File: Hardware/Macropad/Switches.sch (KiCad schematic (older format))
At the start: 49 parts, among them SW1 Rotary_Encoder_Switch, SW10 K21_1U, SW11 K11_1U, SW12 K01_1U, SW13 K42_1U, SW14 K32_1U, SW15 K22_1U, SW16 K12_1U, SW17 K02_1U, SW18 K43_1U, SW19 K33_1U, SW2 K40_1U, SW21 K23_1U, SW22 K13_1U, SW24 K03_1U, SW3 K30_1U, SW4 K20_1U, SW5 K10_1U, SW7 K00_1U, SW8 K41_1U, SW9 K31_1U

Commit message: Schematic mostly done. Started grouping components in layout
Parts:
- D10: renamed from D20; footprint Diode_SMD:D_SOD-323F -> custom_footprint_library:SOD323_HS
- D11: renamed from D23; footprint Diode_SMD:D_SOD-323F -> custom_footprint_library:SOD323_HS
- D12: renamed from D24; footprint Diode_SMD:D_SOD-323F -> custom_footprint_library:SOD323_HS
- D13: renamed from D25; footprint Diode_SMD:D_SOD-323F -> custom_footprint_library:SOD323_HS
- D14: renamed from D26; footprint Diode_SMD:D_SOD-323F -> custom_footprint_library:SOD323_HS
- D15: renamed from D27; footprint Diode_SMD:D_SOD-323F -> custom_footprint_library:SOD323_HS
- D16: renamed from D28; footprint Diode_SMD:D_SOD-323F -> custom_footprint_library:SOD323_HS
- D17: renamed from D29; footprint Diode_SMD:D_SOD-323F -> custom_footprint_library:SOD323_HS
- D18: renamed from D30; footprint Diode_SMD:D_SOD-323F -> custom_footprint_library:SOD323_HS
- D19: renamed from D31; footprint Diode_SMD:D_SOD-323F -> custom_footprint_library:SOD323_HS
- D2: renamed from D3; footprint Diode_SMD:D_SOD-323F -> custom_footprint_library:SOD323_HS
- D20: renamed from D32; footprint Diode_SMD:D_SOD-323F -> custom_footprint_library:SOD323_HS
- D21: renamed from D33; footprint Diode_SMD:D_SOD-323F -> custom_footprint_library:SOD323_HS
- D22: renamed from D2; footprint Diode_SMD:D_SOD-323F -> custom_footprint_library:SOD323_HS
- D3: renamed from D4; footprint Diode_SMD:D_SOD-323F -> custom_footprint_library:SOD323_HS
- D4: renamed from D5; footprint Diode_SMD:D_SOD-323F -> custom_footprint_library:SOD323_HS
- D5: renamed from D6; footprint Diode_SMD:D_SOD-323F -> custom_footprint_library:SOD323_HS
- D6: renamed from D7; footprint Diode_SMD:D_SOD-323F -> custom_footprint_library:SOD323_HS
- D7: renamed from D8; footprint Diode_SMD:D_SOD-323F -> custom_footprint_library:SOD323_HS
- D8: renamed from D9; footprint Diode_SMD:D_SOD-323F -> custom_footprint_library:SOD323_HS
- D9: renamed from D10; footprint Diode_SMD:D_SOD-323F -> custom_footprint_library:SOD323_HS
- H1, H2, H3, H4: renamed from H?; footprint (none) -> mounting_hole:MountingHole_3.2mm_M3_ISO7380_Pad
- J2: renamed from J?; footprint (none) -> Connector_PinSocket_2.54mm:PinSocket_1x04_P2.54mm_Vertical
- renumbered R4 to R13, R3 to R14, SW2 to SW1, SW12 to SW10, SW13 to SW11, SW14 to SW12, SW15 to SW13, SW16 to SW14, SW17 to SW15, SW18 to SW16, SW19 to SW17, SW21 to SW18, SW22 to SW19, SW3 to SW2, SW24 to SW20, SW1 to SW21, SW4 to SW3, SW5 to SW4, SW7 to SW5, SW8 to SW6, SW9 to SW7, SW10 to SW8, SW11 to SW9

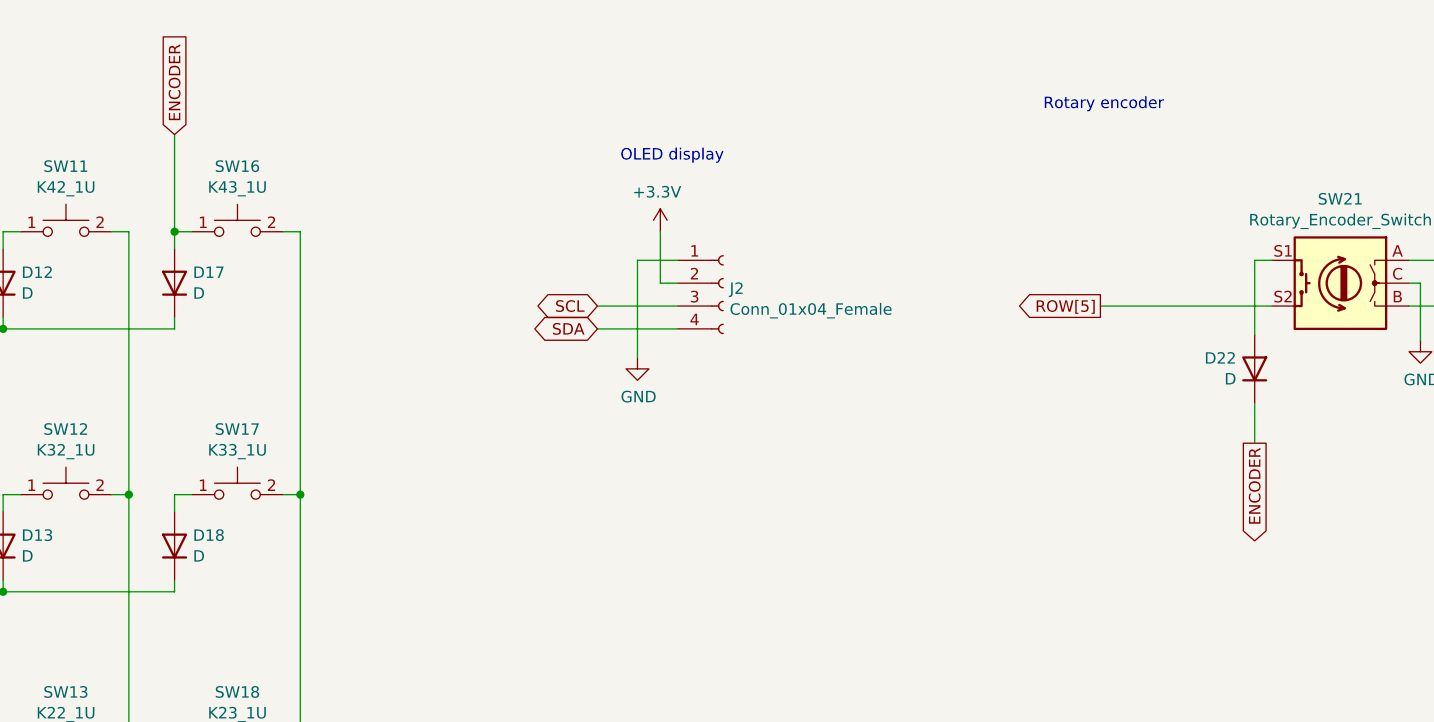
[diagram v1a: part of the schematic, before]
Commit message: Redoing layout with key switches upside down for better LED placement
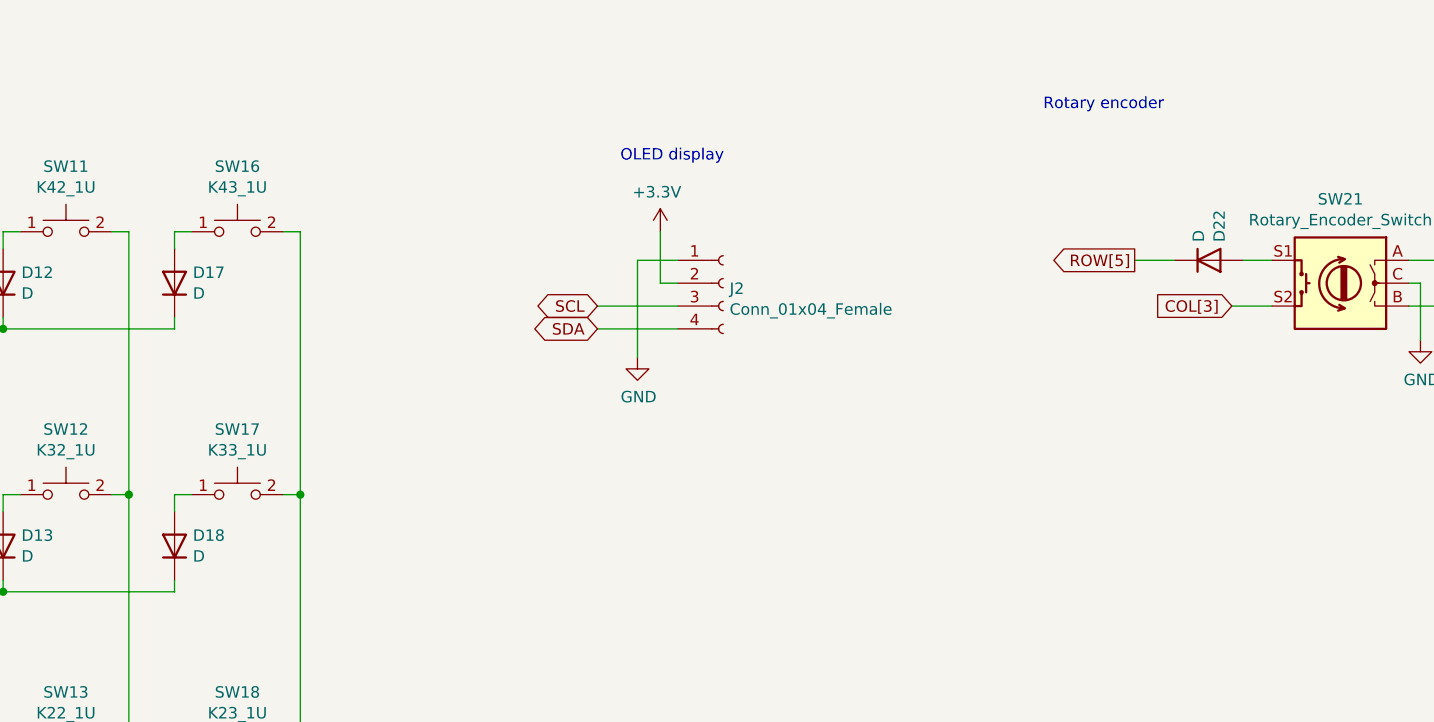
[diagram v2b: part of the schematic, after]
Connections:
- net COL[3]: now also SW21.S2
- net ROW[5]: now also D22.1 (K); no longer SW21.S2
- net ENCODER: no longer names the net of D17.2 (A), SW16.1
- net ENCODER: no longer D22.1 (K)
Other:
- moved on the sheet: D22
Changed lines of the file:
@@
 L Device:D D22
 U 1 1 61C4D1B7
-P 9000 2100
-F 0 "D22" V 9046 2020 50  0000 R CNN
-F 1 "D" V 8955 2020 50  0000 R CNN
-F 2 "custom_footprint_library:SOD323_HS" H 9000 2100 50  0001 C CNN
-F 3 "~" H 9000 2100 50  0001 C CNN
-	1    9000 2100
-	0    1    -1   0
+P 8800 1625
+F 0 "D22" V 8846 1545 50  0000 R CNN
+F 1 "D" V 8755 1545 50  0000 R CNN
+F 2 "custom_footprint_library:SOD323_HS" H 8800 1625 50  0001 C CNN
+F 3 "~" H 8800 1625 50  0001 C CNN
+	1    8800 1625
+	1    0    0    1
 $EndComp
 $Comp
@@
 Wire Wire Line
 	2575 4950 2575 6100
-Text GLabel 8325 1825 0    50   Output ~ 0
+Text GLabel 8475 1625 0    50   Output ~ 0
 ROW[5]
-Wire Wire Line
-	9075 1825 8325 1825
-Wire Wire Line
-	9075 1625 9000 1625
-Wire Wire Line
-	9000 1625 9000 1950
-Text GLabel 9000 2425 3    50   Output ~ 0
-ENCODER
-Wire Wire Line
-	9000 2425 9000 2250
-Text GLabel 4275 1075 1    50   Input ~ 0
-ENCODER
-Wire Wire Line
-	4275 1075 4275 1500
-Connection ~ 4275 1500
 Wire Wire Line
 	9675 1625 10150 1625
@@
 Text Notes 8075 975  0    50   ~ 0
 Rotary encoder
+Text GLabel 8900 1825 0    50   Input ~ 0
+COL[3]
+Wire Wire Line
+	8475 1625 8650 1625
+Wire Wire Line
+	8950 1625 9075 1625
+Wire Wire Line
+	8900 1825 9075 1825
 $EndSCHEMATC

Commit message: Layout done, cleaned up schematic and generated gerbers
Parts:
- added R12, R17: 4K7, resistor_smd:R_0603_1608Metric, symbol Device:R
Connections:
- net +3V3: now also R12.1, R17.1
- net SCL: now also R12.2
- net SDA: now also R17.2
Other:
- moved on the sheet: H1, H2, H3, H4, J2
